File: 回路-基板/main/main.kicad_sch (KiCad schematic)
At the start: 5 parts, among them J1 Conn_01x02_Pin, U1 TWE-L-WX

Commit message: 回路やったぜぇ
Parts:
- added C4, C5: 10uF, symbol Device:C_Small
- added J2: Conn_01x06_Pin, symbol Connector:Conn_01x06_Pin
- added R1, R3, R4, R6, R8: 100k, symbol Device:R_Small
- added R2: 10k, symbol Device:R_Small
- added SW1, SW2, SW3, SW4, SW5: SW_Push, symbol Switch:SW_Push
- added U2: ~, symbol CanSat:Display-I2C
- added U3: LM1117MP-3.3, Package_TO_SOT_SMD:SOT-223-3_TabPin2, symbol Regulator_Linear:LM1117MP-3.3
- added U4: ~, symbol CanSat:GY-NEO6MV2
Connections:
- net GND: now also C4.2, C5.2, J2.1 (Pin_1), R1.1, R3.1, R4.1, R6.1, R8.1, U2.1 (GND), U3.1 (GND), U4.4 (GND)
- net RX=main: now also J2.5 (Pin_5), U4.3 (TX)
- net SCL: now also U2.3 (SCL)
- net SDA: now also U2.4 (SDA)
- net TX=main: now also J2.4 (Pin_4), U4.2 (RX)
- net VCC: now also C4.1, U3.3 (VI); no longer U1.5 (VCC)
- net SPI-CLK: now reaches U1.1 (DO0/PWM2)
- net SPI-MISO: now reaches U1.2 (DO1/PWM3)
- net SPI-MOSI: now reaches U1.3 (DIO18/DO1)
- net CTS=main: now reaches U1.6 (DIO4/DO3)
- net CTS=main: now also J2.2 (Pin_2)
- net RTS=main: now reaches U1.7 (DIO5/PWM1)
- net RTS=main: now also J2.6 (Pin_6)
- net BTN-B renamed BTN-DOWN
- net BTN-DOWN: now also R8.2, SW4.1
- net BTN-C renamed BTN-CENTER
- net BTN-CENTER: now also R1.2, SW1.1
- net BTN-L renamed BTN-LEFT
- net BTN-LEFT: now also R6.2, SW3.1
- net BTN-R renamed BTN-RIGHT
- net BTN-RIGHT: now also R4.2, SW5.1
- net BTN-T renamed BTN-UP
- net BTN-UP: now also R3.2, SW2.1
- new net: R2.2, SW1.2, SW2.2, SW3.2, SW4.2, SW5.2
- new net +3.3V: C5.1, R2.1, U1.5 (VCC), U2.2 (VCC), U3.2 (VO), U4.1 (VCC)
- no-connect marks 0 -> 1
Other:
- note added: "BUTTON"
- note added: "DISPLAY"
- note added: "GPS"
- note added: "MPU|TWE-LITE"
- note added: "POWER"
- note added: "USB-Serial"
- moved on the sheet: C1, C2, C3, J1, U1

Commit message: 回路更新
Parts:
- added Q1, Q2, Q3, Q4: 2SC1815, Package_TO_SOT_THT:TO-92_Inline, symbol Transistor_BJT:2SC1815
- added R5: 10k, symbol Device:R_Small
- added R7, R9: 100k, symbol Device:R_Small
- added SW6: SW_SPDT, symbol Switch:SW_SPDT
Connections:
- net +3.3V: now also R5.1
- net GND: now also R7.2, R9.2
- net RX=main: now also Q1.2 (C), Q3.2 (C); no longer J2.5 (Pin_5), U4.3 (TX)
- net TX=main: now also Q2.2 (C), Q4.2 (C); no longer J2.4 (Pin_4), U4.2 (RX)
- new net: R5.2, SW6.2 (B)
- new net GPS-RX=main: Q3.1 (E), U4.3 (TX)
- new net GPS-TX=main: Q4.1 (E), U4.2 (RX)
- new net UART-GPS=ON: Q3.3 (B), Q4.3 (B), R9.1, SW6.3 (C)
- new net UART-USB=ON: Q1.3 (B), Q2.3 (B), R7.1, SW6.1 (A)
- new net USB-RX=main: J2.5 (Pin_5), Q1.1 (E)
- new net USB-TX=main: J2.4 (Pin_4), Q2.1 (E)
- no-connect marks 1 -> 12
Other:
- note added: "UART-SWITCHING"

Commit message: 右下のトランジスタの種類変えたよ
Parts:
- removed Q1, Q2, Q3, Q4: 2SC1815, Package_TO_SOT_THT:TO-92_Inline, symbol Transistor_BJT:2SC1815
- added Q1, Q3: PNP, symbol Simulation_SPICE:PNP
- added Q2, Q4: NPN, symbol Simulation_SPICE:NPN
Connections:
- net GPS-RX=main: now also Q3.3 (E)
- net GPS-TX=main: now also Q4.3 (E)
- net RX=main: now also Q1.1 (C), Q3.1 (C)
- net TX=main: now also Q2.1 (C), Q4.1 (C)
- net UART-GPS=ON: now also Q3.2 (B), Q4.2 (B)
- net UART-USB=ON: now also Q1.2 (B), Q2.2 (B)
- net USB-RX=main: now also Q1.3 (E)
- net USB-TX=main: now also Q2.3 (E)

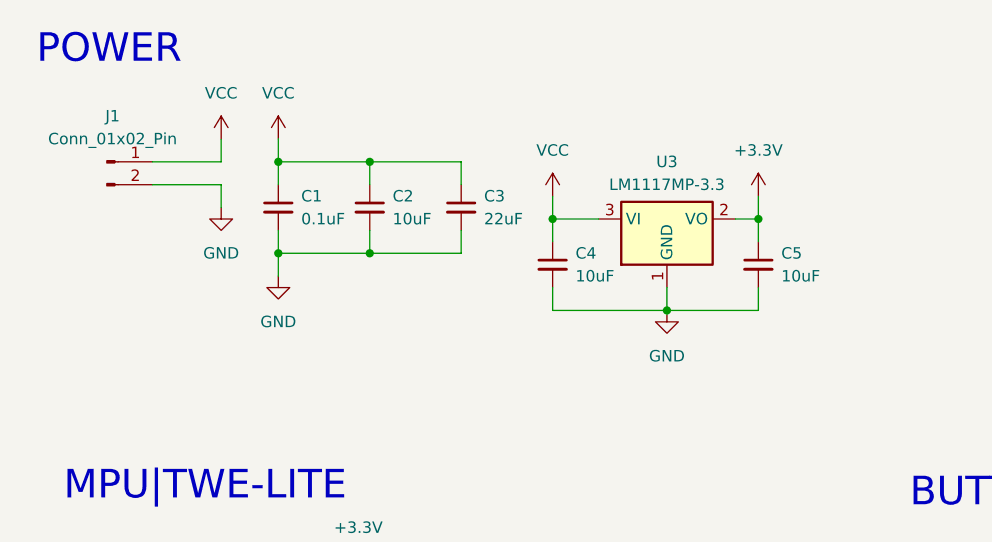
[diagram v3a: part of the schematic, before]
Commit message: 回路の電源部分をバッテリーに変更した
コネクタからバッテリーx2に変更したよ
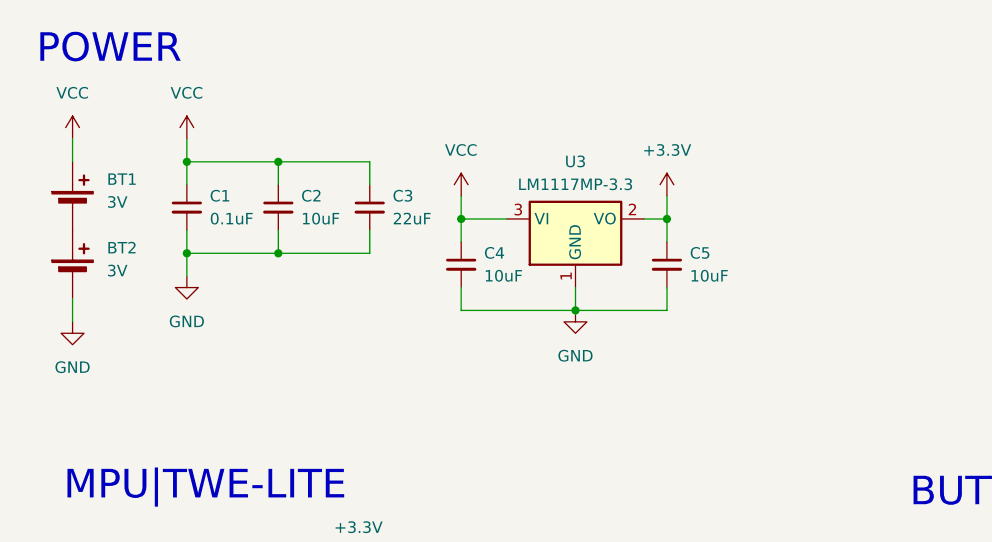
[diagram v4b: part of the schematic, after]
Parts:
- removed J1: Conn_01x02_Pin, symbol Connector:Conn_01x02_Pin
- added BT1, BT2: 3V, symbol Device:Battery_Cell
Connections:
- net GND: now also BT2.2 (-)
- net VCC: now also BT1.1 (+)
- new net: BT1.2 (-), BT2.1 (+)
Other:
- moved on the sheet: C1, C2, C3, C4, C5, U3

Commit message: PCB半分完成
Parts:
- BT1, BT2: footprint (none) -> @2024-cansat:BHSD-2032-SM
- C1, C2, C3, C4, C5: footprint (none) -> Capacitor_SMD:C_0805_2012Metric
- J2: footprint (none) -> Connector_PinSocket_2.54mm:PinSocket_1x06_P2.54mm_Horizontal
- Q1, Q3: footprint (none) -> Package_TO_SOT_SMD:SOT-323_SC-70
- Q2, Q4: footprint (none) -> Package_TO_SOT_SMD:SC-59
- R1, R2, R3, R4, R5, R6, R7, R8, R9: footprint (none) -> Resistor_SMD:R_0805_2012Metric
- SW1, SW2, SW3, SW4, SW5: footprint (none) -> @2024-cansat:TVBP06-B043C
- SW6: footprint (none) -> @2024-cansat:SS12D01G4
- U2: footprint (none) -> Connector_PinSocket_2.54mm:PinSocket_1x04_P2.54mm_Vertical
- U4: footprint (none) -> @2024-cansat:GPS-54D-014
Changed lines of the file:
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@@
 		)
 	)
-	(text_box "RXとTXについてはこのままだと\nプログラム書き込み時にバッティング\nするため必ず変更すること!"
-		(exclude_from_sim no)
-		(at 76.2 168.91 0)
-		(size 33.02 7.62)
-		(stroke
-			(width 0)
-			(type default)
-		)
-		(fill
-			(type none)
-		)
-		(effects
-			(font
-				(face "Yu Gothic")
-				(size 1.27 1.27)
-				(thickness 0.254)
-				(bold yes)
-			)
-			(justify left top)
-		)
-	)
 	(text "DISPLAY"
 		(exclude_from_sim no)
@@
 			)
 		)
-		(property "Footprint" ""
+		(property "Footprint" "@2024-cansat:BHSD-2032-SM"
 			(at 21.59 42.926 90)
 			(effects
@@
 			)
 		)
-		(property "Footprint" ""
+		(property "Footprint" "Resistor_SMD:R_0805_2012Metric"
 			(at 222.25 54.61 0)
 			(effects
@@
 			)
 		)
-		(property "Footprint" ""
+		(property "Footprint" "Package_TO_SOT_SMD:SOT-323_SC-70"
 			(at 280.67 90.17 0)
 			(effects
@@
 	)
 	(symbol
+		(lib_name "Battery_Cell_1")
 		(lib_id "Device:Battery_Cell")
 		(at 21.59 36.83 0)
@@
 			)
 		)
-		(property "Footprint" ""
+		(property "Footprint" "@2024-cansat:BHSD-2032-SM"
 			(at 21.59 35.306 90)
 			(effects
@@
 			)
 		)
-		(property "Footprint" ""
+		(property "Footprint" "@2024-cansat:GPS-54D-014"
 			(at 78.74 155.448 0)
 			(effects
@@
 			)
 		)
-		(property "Footprint" ""
+		(property "Footprint" "Resistor_SMD:R_0805_2012Metric"
 			(at 240.03 63.5 0)
 			(effects
@@
 			)
 		)
-		(property "Footprint" ""
+		(property "Footprint" "Resistor_SMD:R_0805_2012Metric"
 			(at 123.19 113.03 0)
 			(effects
@@
 			)
 		)
-		(property "Footprint" ""
+		(property "Footprint" "@2024-cansat:TVBP06-B043C"
 			(at 135.89 92.71 0)
 			(effects
@@
 			)
 		)
-		(property "Footprint" ""
+		(property "Footprint" "@2024-cansat:SS12D01G4"
 			(at 232.41 54.61 0)
 			(effects
@@
 			)
 		)
-		(property "Footprint" ""
+		(property "Footprint" "@2024-cansat:TVBP06-B043C"
 			(at 135.89 113.03 0)
 			(effects
@@
 			)
 		)
-		(property "Footprint" ""
+		(property "Footprint" "Package_TO_SOT_SMD:SC-59"
 			(at 308.61 148.59 0)
 			(effects
@@
 			)
 		)
-		(property "Footprint" ""
+		(property "Footprint" "Connector_PinSocket_2.54mm:PinSocket_1x04_P2.54mm_Vertical"
 			(at 129.54 152.146 0)
 			(effects
@@
 			)
 		)
-		(property "Footprint" ""
+		(property "Footprint" "Package_TO_SOT_SMD:SC-59"
 			(at 308.61 109.22 0)
 			(effects
@@
 			)
 		)
-		(property "Footprint" ""
+		(property "Footprint" "Connector_PinSocket_2.54mm:PinSocket_1x06_P2.54mm_Horizontal"
 			(at 29.21 163.83 0)
 			(effects
@@
 			)
 		)
-		(property "Footprint" ""
+		(property "Footprint" "Resistor_SMD:R_0805_2012Metric"
 			(at 242.57 63.5 0)
 			(effects
@@
 			)
 		)
-		(property "Footprint" ""
+		(property "Footprint" "Resistor_SMD:R_0805_2012Metric"
 			(at 123.19 123.19 0)
 			(effects
@@
 			)
 		)
-		(property "Footprint" ""
+		(property "Footprint" "@2024-cansat:TVBP06-B043C"
 			(at 135.89 82.55 0)
 			(effects
@@
 			)
 		)
-		(property "Footprint" ""
+		(property "Footprint" "Resistor_SMD:R_0805_2012Metric"
 			(at 123.19 82.55 0)
 			(effects
@@
 			)
 		)
-		(property "Footprint" ""
+		(property "Footprint" "@2024-cansat:TVBP06-B043C"
 			(at 135.89 72.39 0)
 			(effects
@@
 			)
 		)
-		(property "Footprint" ""
+		(property "Footprint" "Capacitor_SMD:C_0805_2012Metric"
 			(at 64.77 43.18 0)
 			(effects
@@
 			)
 		)
-		(property "Footprint" ""
+		(property "Footprint" "Capacitor_SMD:C_0805_2012Metric"
 			(at 54.61 36.83 0)
 			(effects
@@
 			)
 		)
-		(property "Footprint" ""
+		(property "Footprint" "Package_TO_SOT_SMD:SOT-323_SC-70"
 			(at 280.67 129.54 0)
 			(effects
@@
 			)
 		)
-		(property "Footprint" ""
+		(property "Footprint" "Resistor_SMD:R_0805_2012Metric"
 			(at 123.19 92.71 0)
 			(effects
@@
 			)
 		)
-		(property "Footprint" ""
+		(property "Footprint" "Capacitor_SMD:C_0805_2012Metric"
 			(at 44.45 36.83 0)
 			(effects
@@
 			)
 		)
-		(property "Footprint" ""
+		(property "Footprint" "Capacitor_SMD:C_0805_2012Metric"
 			(at 34.29 36.83 0)
 			(effects
@@
 			)
 		)
-		(property "Footprint" ""
+		(property "Footprint" "Resistor_SMD:R_0805_2012Metric"
 			(at 123.19 102.87 0)
 			(effects
@@
 			)
 		)
-		(property "Footprint" ""
+		(property "Footprint" "Capacitor_SMD:C_0805_2012Metric"
 			(at 87.63 43.18 0)
 			(effects
@@
 			)
 		)
-		(property "Footprint" ""
+		(property "Footprint" "@2024-cansat:TVBP06-B043C"
 			(at 135.89 102.87 0)
 			(effects
@@
 			)
 		)
-		(property "Footprint" ""
+		(property "Footprint" "Resistor_SMD:R_0805_2012Metric"
 			(at 143.51 72.39 0)
 			(effects

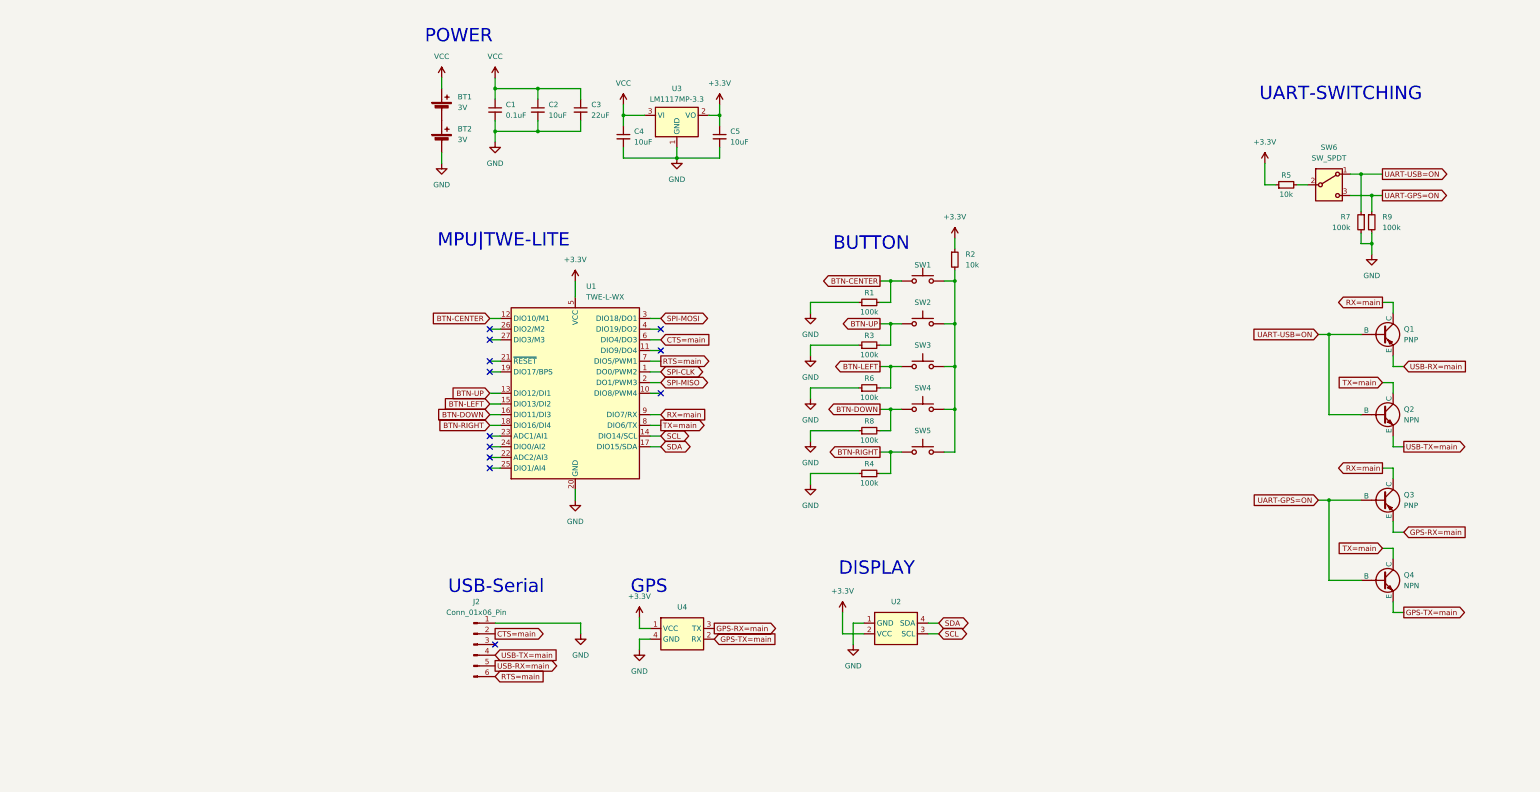
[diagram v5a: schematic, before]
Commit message: 回路やり直したよ
山本さんからのアドバイス部分を修正
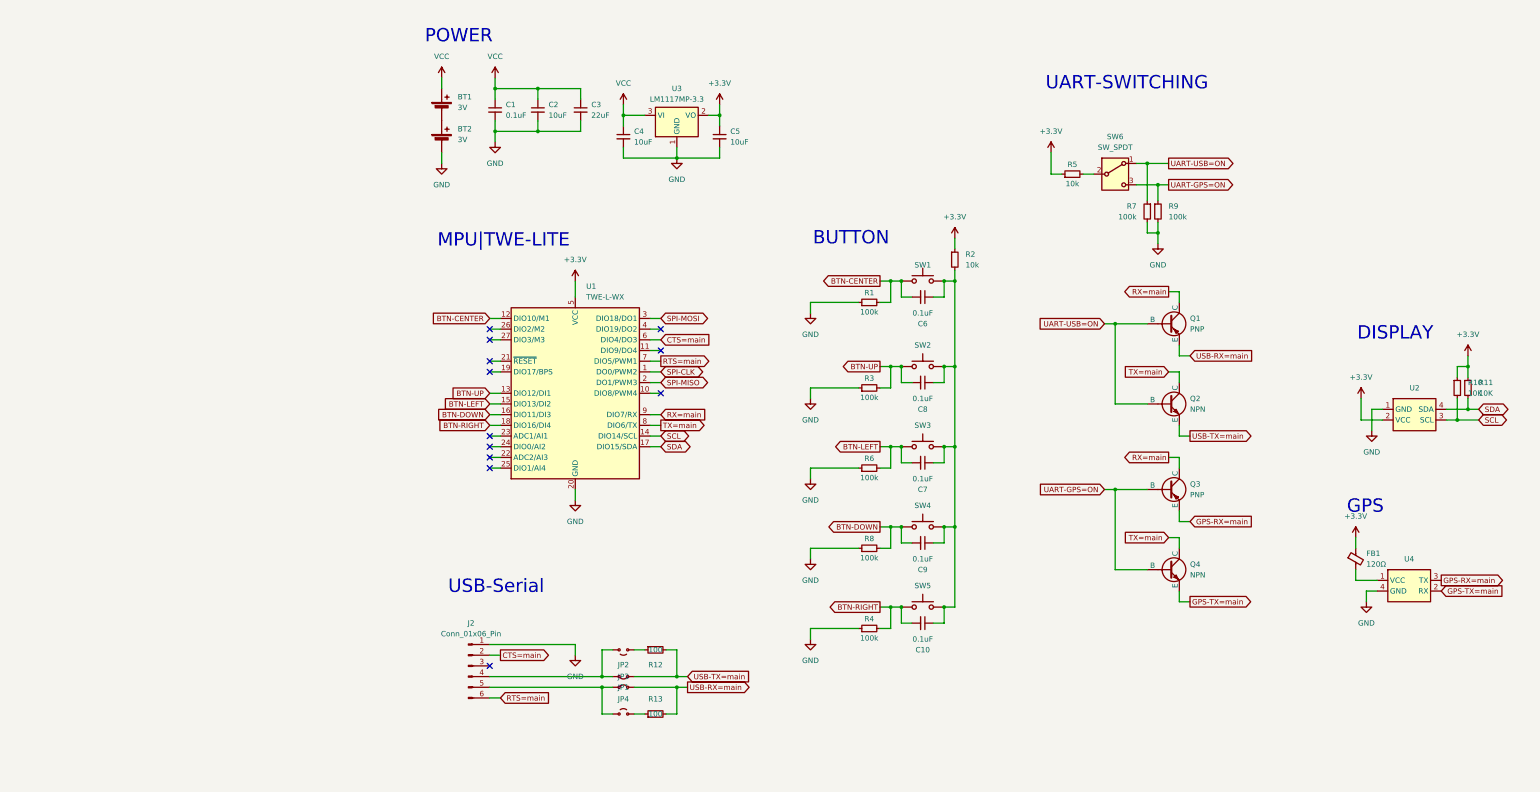
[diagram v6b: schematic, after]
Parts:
- added C10, C6, C7, C8, C9: 0.1uF, symbol Device:C_Small
- added FB1: 120Ω, symbol Device:FerriteBead_Small
- added JP1, JP3: Jumper_2_Small_Bridged, symbol Jumper:Jumper_2_Small_Bridged
- added JP2, JP4: Jumper_2_Small_Open, symbol Jumper:Jumper_2_Small_Open
- added R10, R11: 10K, symbol Device:R_Small
- added R12, R13: 100, symbol Device:R_Small
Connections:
- net +3.3V: now also FB1.1, R10.1, R11.1; no longer U4.1 (VCC)
- net BTN-CENTER: now also C6.2
- net BTN-DOWN: now also C9.2
- net BTN-LEFT: now also C7.2
- net BTN-RIGHT: now also C10.2
- net BTN-UP: now also C8.2
- net SCL: now also R10.2
- net SDA: now also R11.2
- net USB-RX=main: now also JP3.2 (B), R13.2; no longer J2.5 (Pin_5)
- net USB-TX=main: now also JP1.2 (B), R12.2; no longer J2.4 (Pin_4)
- net at R2.2, SW1.2, SW2.2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: now also C10.1, C6.1, C7.1, C8.1, C9.1
- new net: FB1.2, U4.1 (VCC)
- new net: JP2.2 (B), R12.1
- new net: J2.4 (Pin_4), JP1.1 (A), JP2.1 (A)
- new net: J2.5 (Pin_5), JP3.1 (A), JP4.1 (A)
- new net: JP4.2 (B), R13.1
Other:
- moved on the sheet: J2, Q1, Q2, Q3, Q4, R3, R4, R5, R6, R7, R8, R9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

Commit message: 回路関連
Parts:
- removed U4: ~, @2024-cansat:GPS-54D-014, symbol CanSat:GY-NEO6MV2
- added U4: ~, @2024-cansat:GPS-54D-014, symbol @cansat:GPS-54DB-014
- C10, C6, C7, C8, C9: footprint (none) -> Capacitor_SMD:C_0805_2012Metric
- FB1: footprint (none) -> Inductor_SMD:L_0603_1608Metric
- JP1, JP3: footprint (none) -> Jumper:SolderJumper-2_P1.3mm_Bridged_Pad1.0x1.5mm
- JP2, JP4: footprint (none) -> Jumper:SolderJumper-2_P1.3mm_Open_Pad1.0x1.5mm
- R10, R11, R12, R13: footprint (none) -> Resistor_SMD:R_0805_2012Metric
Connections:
- net GND: now also U4.2 (GND)
- net GPS-RX=main: now also U4.3 (TX)
- net GPS-TX=main: now also U4.1 (RX)
- net at FB1.2: now also U4.5 (VCC)
- no-connect marks 12 -> 16
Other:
- moved on the sheet: FB1
